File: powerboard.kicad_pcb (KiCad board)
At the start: 2 copper layers, 81.3 x 61.6 mm, 26 parts, among them J1 B03B, J2 EMER_SW, J3 EMER_SW, Q1 TJ60S04M3L, U1 TLP222A

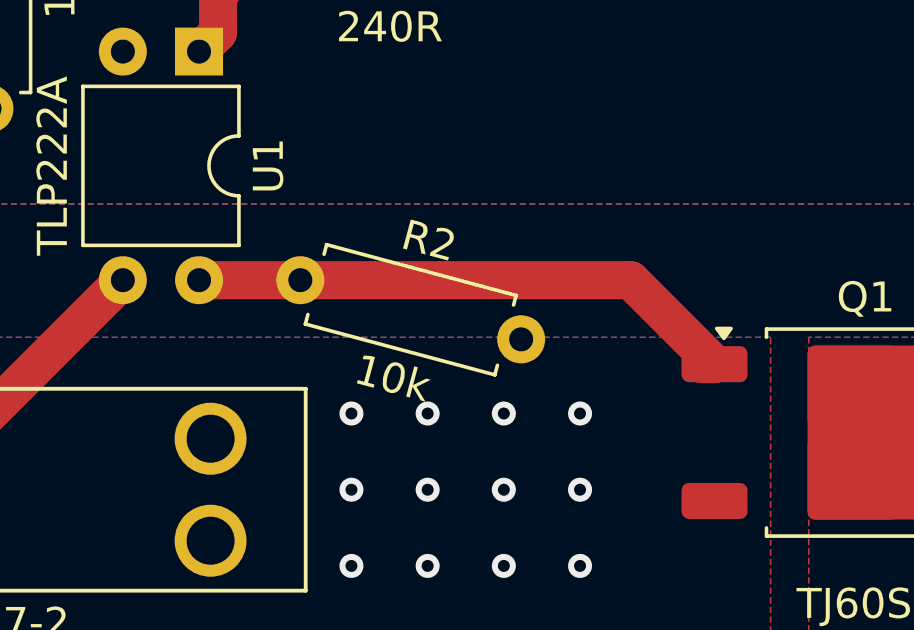
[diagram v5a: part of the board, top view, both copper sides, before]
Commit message: pcb: change angle of CUTE RESISTOR
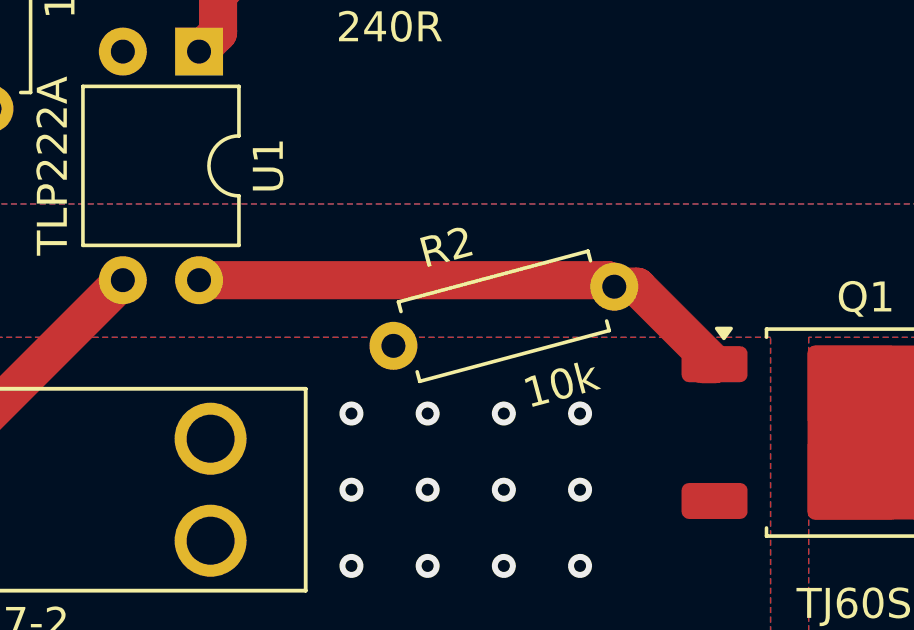
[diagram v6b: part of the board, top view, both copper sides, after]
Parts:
- moved R2 4.26 mm to (155.7, 115.9), turned to 15 degrees
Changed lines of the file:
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@@
 	(footprint "Resistor_THT:R_Axial_DIN0207_L6.3mm_D2.5mm_P7.62mm_Horizontal"
 		(layer "F.Cu")
-		(at 159.962117 115.637201 165)
+		(at 155.704823 115.853899 15)
 		(descr "Resistor, Axial_DIN0207 series, Axial, Horizontal, pin pitch=7.62mm, 0.25W = 1/4W, length*diameter=6.3*2.5mm^2, http://cdn-reichelt.de/documents/datenblatt/B400/1_4W%23YAG.pdf")
 		(tags "Resistor Axial_DIN0207 series Axial Horizontal pin pitch 7.62mm 0.25W = 1/4W length 6.3mm diameter 2.5mm")
 		(property "Reference" "R2"
-			(at 3.81 2.37 -15)
+			(at 2.562411 -2.704291 15)
 			(layer "F.SilkS")
 			(effects
@@
 		)
 		(property "Value" "10k"
-			(at 3.81 -2.37 -15)
+			(at 5.057588 2.704291 15)
 			(layer "F.SilkS")
 			(effects
@@
 		)
 		(property "Footprint" "Resistor_THT:R_Axial_DIN0207_L6.3mm_D2.5mm_P7.62mm_Horizontal"
-			(at 0 0 165)
+			(at 0 0 15)
 			(unlocked yes)
 			(layer "F.Fab")
@@
 		)
 		(property "Datasheet" ""
-			(at 0 0 165)
+			(at 0 0 15)
 			(unlocked yes)
 			(layer "F.Fab")
@@
 		)
 		(property "Description" ""
-			(at 0 0 165)
+			(at 0 0 15)
 			(unlocked yes)
 			(layer "F.Fab")
@@
 		(attr through_hole)
 		(fp_line
-			(start 7.08 -1.37)
-			(end 7.08 -1.04)
+			(start 0.539999 -1.370001)
+			(end 7.08 -1.370001)
 			(stroke
 				(width 0.12)
@@
 		)
 		(fp_line
-			(start 7.08 1.370001)
-			(end 7.08 1.04)
+			(start 0.54 -1.039999)
+			(end 0.539999 -1.370001)
 			(stroke
 				(width 0.12)
@@
 		)
 		(fp_line
-			(start 0.54 -1.370001)
-			(end 7.08 -1.37)
+			(start 0.54 1.04)
+			(end 0.540001 1.37)
 			(stroke
 				(width 0.12)
@@
 		)
 		(fp_line
-			(start 0.539999 -1.039999)
-			(end 0.54 -1.370001)
+			(start 0.540001 1.37)
+			(end 7.080001 1.370001)
 			(stroke
 				(width 0.12)
@@
 		)
 		(fp_line
-			(start 0.54 1.04)
-			(end 0.540001 1.37)
+			(start 7.08 -1.370001)
+			(end 7.08 -1.04)
 			(stroke
 				(width 0.12)
@@
 		)
 		(fp_line
-			(start 0.540001 1.37)
-			(end 7.08 1.370001)
+			(start 7.080001 1.370001)
+			(end 7.08 1.04)
 			(stroke
 				(width 0.12)
@@
 		)
 		(fp_line
-			(start 8.669999 -1.5)
-			(end -1.050001 -1.5)
+			(start -1.05 -1.5)
+			(end -1.050001 1.5)
 			(stroke
 				(width 0.05)
@@
 		)
 		(fp_line
-			(start 8.67 1.5)
-			(end 8.669999 -1.5)
+			(start -1.050001 1.5)
+			(end 8.669999 1.5)
 			(stroke
 				(width 0.05)
@@
 		)
 		(fp_line
-			(start -1.050001 -1.5)
-			(end -1.05 1.5)
+			(start 8.67 -1.5)
+			(end -1.05 -1.5)
 			(stroke
 				(width 0.05)
@@
 		)
 		(fp_line
-			(start -1.05 1.5)
-			(end 8.67 1.5)
+			(start 8.669999 1.5)
+			(end 8.67 -1.5)
 			(stroke
 				(width 0.05)
@@
 		)
 		(fp_line
-			(start 7.62 0)
-			(end 6.96 -0.000001)
+			(start 0 0)
+			(end 0.66 0.000001)
 			(stroke
 				(width 0.1)
@@
 		)
 		(fp_line
-			(start 6.959999 -1.25)
-			(end 0.66 -1.25)
+			(start 0.66 -1.25)
+			(end 0.66 1.25)
 			(stroke
 				(width 0.1)
@@
 		)
 		(fp_line
-			(start 6.96 1.25)
-			(end 6.959999 -1.25)
+			(start 0.66 1.25)
+			(end 6.96 1.25)
 			(stroke
 				(width 0.1)
@@
 		)
 		(fp_line
-			(start 0.66 -1.25)
-			(end 0.66 1.25)
+			(start 6.959999 -1.25)
+			(end 0.66 -1.25)
 			(stroke
 				(width 0.1)
@@
 		)
 		(fp_line
-			(start 0.66 1.25)
-			(end 6.96 1.25)
+			(start 6.96 1.25)
+			(end 6.959999 -1.25)
 			(stroke
 				(width 0.1)
@@
 		)
 		(fp_line
-			(start 0 0)
-			(end 0.66 0)
+			(start 7.62 0)
+			(end 6.96 0)
 			(stroke
 				(width 0.1)
@@
 		)
 		(fp_text user "${REFERENCE}"
-			(at 3.81 -0.000001 -15)
+			(at 3.810001 0 15)
 			(layer "F.Fab")
 			(effects
@@
 		)
 		(pad "1" thru_hole circle
-			(at 0 0 165)
+			(at 0 0 15)
 			(size 1.6 1.6)
 			(drill 0.8)
@@
 		)
 		(pad "2" thru_hole oval
-			(at 7.62 0 165)
+			(at 7.62 0 15)
 			(size 1.6 1.6)
 			(drill 0.8)
@@
 	)
 	(segment
-		(start 149.225 113.665)
-		(end 152.4 113.665)
+		(start 162.84848 113.665)
+		(end 163.065178 113.881698)
 		(width 1.27)
 		(layer "F.Cu")
@@
 	)
 	(segment
-		(start 163.61 113.665)
+		(start 165.995 116.465)
 		(end 166.41 116.465)
 		(width 1.27)
@@
 	)
 	(segment
-		(start 152.601762 113.665)
-		(end 163.61 113.665)
+		(start 163.826698 113.881698)
+		(end 166.41 116.465)
 		(width 1.27)
 		(layer "F.Cu")
@@
 	)
 	(segment
-		(start 165.995 116.465)
-		(end 166.41 116.465)
+		(start 149.225 113.665)
+		(end 162.84848 113.665)
+		(width 1.27)
+		(layer "F.Cu")
+		(net 9)
+	)
+	(segment
+		(start 163.065178 113.881698)
+		(end 163.826698 113.881698)
 		(width 1.27)
 		(layer "F.Cu")

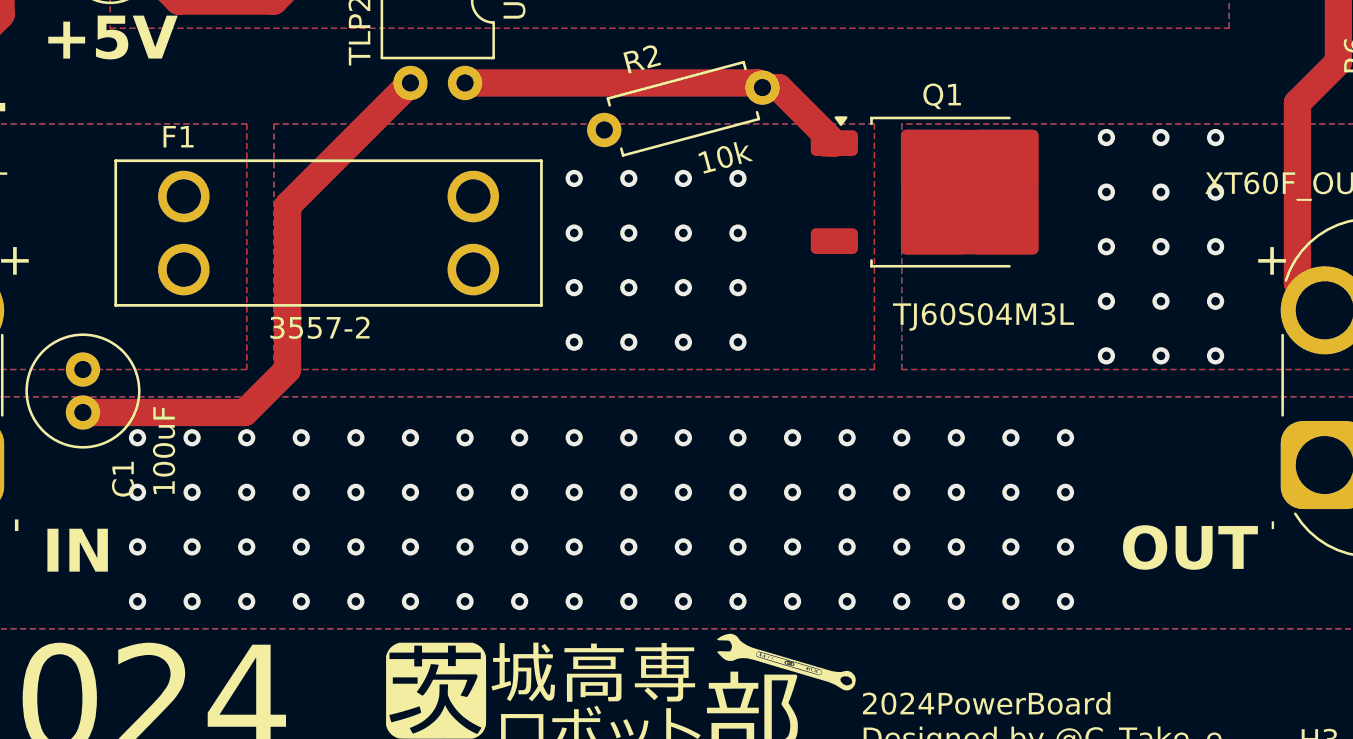
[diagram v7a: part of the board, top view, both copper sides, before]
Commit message: pcb: put vias under FET
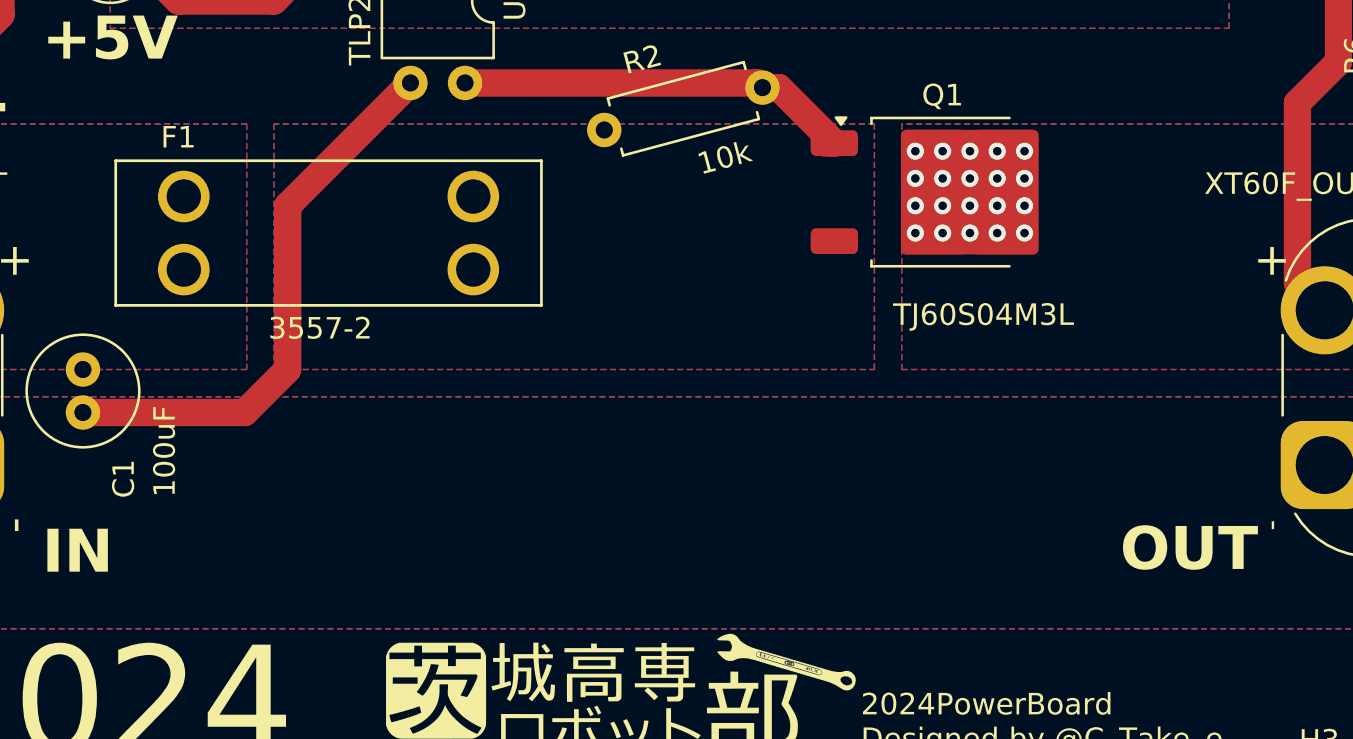
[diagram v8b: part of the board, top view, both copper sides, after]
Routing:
- net VOUT: vias 15 -> 20
- net VDD: vias 16 -> 0
- net GNDPWR: vias 72 -> 0
